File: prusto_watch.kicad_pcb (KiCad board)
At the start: 2 copper layers, 37.4 x 37.4 mm, 56 parts, among them J1 USB_microB_2040002-1, J2 Conn_02x05_Odd_Even, J3 Vibration Motor, J4 Conn_01x06, J5 Conn_01x06, J6 Conn_02x03_Odd_Even, J7 Conn_02x03_Counter_Clockwise, Q3 RUM002N02T2L, U1 STM32F303RCT6-48, U2 LTC4063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

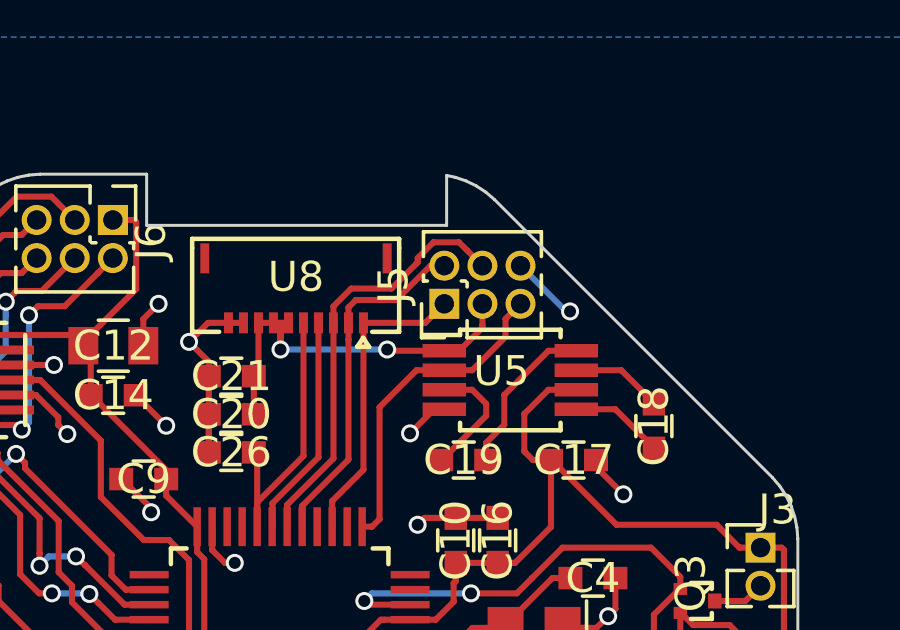
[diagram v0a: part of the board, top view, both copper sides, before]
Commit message: Breakout EXTCOMIN instead of 5Ven
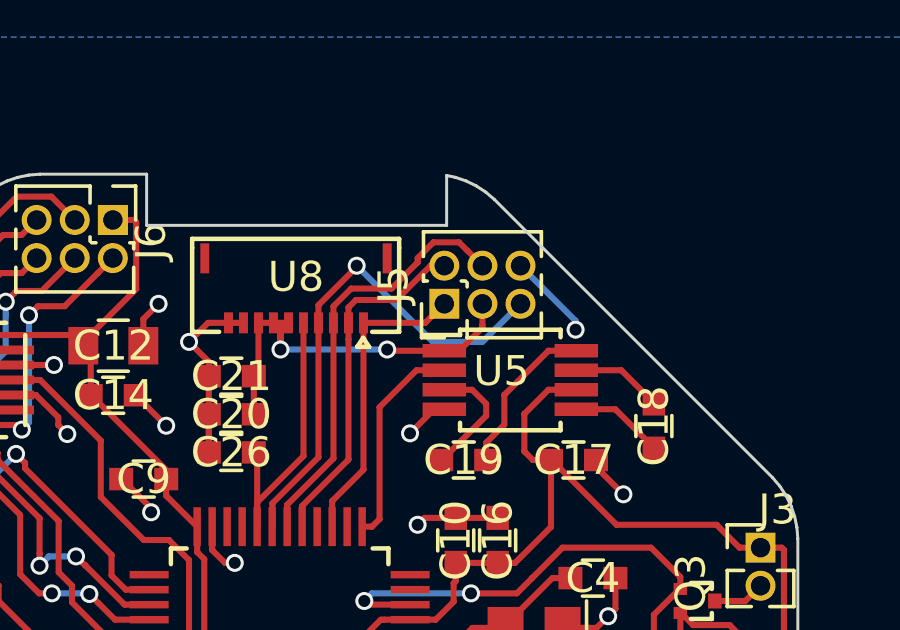
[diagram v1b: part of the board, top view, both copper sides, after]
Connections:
- J5 pad 5: /5V_EN -> /EXTCOMIN
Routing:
- net /EXTCOMIN: track 7.43 -> 17.1 mm, vias 0 -> 1
- net /5V_EN: track 10.9 -> 7.08 mm
- net GND: track 99.6 -> 100.2 mm
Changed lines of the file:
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@@
 (kicad_pcb (version 4) (host pcbnew 4.0.7)
   (general
-    (links 0)
+    (links 169)
     (no_connects 0)
     (area 127.356999 80.719059 164.868201 118.230261)
     (thickness 1.6)
     (drawings 80)
-    (tracks 791)
+    (tracks 795)
     (zones 0)
     (modules 56)
@@
       (net 26 /DISP_SCS))
     (pad 5 thru_hole oval (at 0 2.54 90) (size 1 1) (drill 0.65) (layers *.Cu *.Mask)
-      (net 30 /5V_EN))
+      (net 29 /EXTCOMIN))
     (pad 6 thru_hole oval (at 1.27 2.54 90) (size 1 1) (drill 0.65) (layers *.Cu *.Mask)
       (net 2 GND))
@@
       (xy -0.113933 2.757629) (xy -0.013056 2.757714) (xy 0 2.757714) (xy 0.10391 2.757652)) (layer B.SilkS) (width 0.01))
   )
-  (gr_text "Prusto Watch\nV0.4\nByron Wasti" (at 153.416 94.488 360) (layer B.SilkS)
+  (gr_text "Prusto Watch\nV0.4\nByron Wasti" (at 153.416 94.488) (layer B.SilkS)
     (effects (font (size 1.5 1.5) (thickness 0.3)) (justify left mirror))
   )
@@
     (effects (font (size 0.762 0.762) (thickness 0.1905)) (justify mirror))
   )
-  (gr_text GND (at 161.798 94.488 360) (layer B.SilkS)
+  (gr_text GND (at 161.798 94.488) (layer B.SilkS)
     (effects (font (size 0.762 0.762) (thickness 0.1905)) (justify mirror))
   )
@@
     (effects (font (size 0.762 0.762) (thickness 0.1905)) (justify mirror))
   )
-  (gr_text GND (at 130.302 94.742 360) (layer B.SilkS)
+  (gr_text GND (at 130.302 94.742) (layer B.SilkS)
     (effects (font (size 0.762 0.762) (thickness 0.1905)) (justify mirror))
   )
@@
   (segment (start 133.08 91.9425) (end 133.4332 91.9425) (width 0.2032) (layer F.Cu) (net 1))
   (via (at 133.785433 92.335751) (size 0.6) (drill 0.4) (layers F.Cu B.Cu) (net 1))
+  (segment (start 157.410267 85.655267) (end 157.410267 85.952188) (width 0.2032) (layer B.Cu) (net 2))
+  (segment (start 155.575 83.82) (end 157.410267 85.655267) (width 0.2032) (layer B.Cu) (net 2))
+  (via (at 157.410267 85.952188) (size 0.6) (drill 0.4) (layers F.Cu B.Cu) (net 2))
   (segment (start 157.969948 112.032051) (end 156.21 113.791999) (width 0.2032) (layer F.Cu) (net 2))
   (segment (start 156.21 113.791999) (end 156.21 114.3) (width 0.2032) (layer F.Cu) (net 2))
@@
   (via (at 144.526 86.36) (size 0.6) (drill 0.4) (layers F.Cu B.Cu) (net 2))
   (via (at 159.004 91.44) (size 0.6) (drill 0.4) (layers F.Cu B.Cu) (net 2))
-  (via (at 157.226 85.344) (size 0.6) (drill 0.4) (layers F.Cu B.Cu) (net 2))
   (via (at 151.892 89.408) (size 0.6) (drill 0.4) (layers F.Cu B.Cu) (net 2))
   (via (at 158.496 95.504) (size 0.6) (drill 0.4) (layers F.Cu B.Cu) (net 2))
@@
   (segment (start 142.144926 102.084) (end 142.388464 101.840462) (width 0.2032) (layer F.Cu) (net 2))
   (segment (start 163.83 106.7482) (end 162.8822 107.696) (width 0.2032) (layer F.Cu) (net 2))
-  (segment (start 157.099 85.344) (end 157.226 85.344) (width 0.2032) (layer B.Cu) (net 2))
   (segment (start 145.161 85.725) (end 144.526 86.36) (width 0.2032) (layer F.Cu) (net 2))
   (segment (start 163.83 106.045) (end 163.83 106.7482) (width 0.2032) (layer F.Cu) (net 2))
   (segment (start 132.7 93.205) (end 132.7 93.98) (width 0.2032) (layer F.Cu) (net 2))
-  (segment (start 155.575 83.82) (end 157.099 85.344) (width 0.2032) (layer B.Cu) (net 2))
   (segment (start 141.478 102.084) (end 142.144926 102.084) (width 0.2032) (layer F.Cu) (net 2))
   (segment (start 142.388464 101.840462) (end 142.688463 101.540463) (width 0.2032) (layer F.Cu) (net 2))
@@
   (segment (start 150.34 90.6218) (end 150.34 86.2782) (width 0.2032) (layer F.Cu) (net 28))
   (segment (start 150.34 86.2782) (end 150.34 85.725) (width 0.2032) (layer F.Cu) (net 28))
+  (segment (start 152.654 86.36) (end 154.305 86.36) (width 0.2032) (layer B.Cu) (net 29))
+  (segment (start 154.305 86.36) (end 155.575 85.09) (width 0.2032) (layer B.Cu) (net 29))
+  (segment (start 155.448 85.217) (end 155.575 85.09) (width 0.2032) (layer F.Cu) (net 29))
+  (segment (start 150.114 83.82) (end 152.654 86.36) (width 0.2032) (layer B.Cu) (net 29))
+  (segment (start 148.84 85.725) (end 148.84 85.132973) (width 0.2032) (layer F.Cu) (net 29))
+  (segment (start 148.84 85.132973) (end 150.114 83.858973) (width 0.2032) (layer F.Cu) (net 29))
+  (segment (start 150.114 83.858973) (end 150.114 83.82) (width 0.2032) (layer F.Cu) (net 29))
+  (via (at 150.114 83.82) (size 0.6) (drill 0.4) (layers F.Cu B.Cu) (net 29))
   (segment (start 148.84 85.725) (end 148.84 90.204831) (width 0.2032) (layer F.Cu) (net 29))
   (segment (start 148.84 90.204831) (end 147.305375 91.739456) (width 0.2032) (layer F.Cu) (net 29))
@@
   (segment (start 150.296 92.519) (end 150.6242 92.519) (width 0.2032) (layer F.Cu) (net 30))
   (segment (start 150.6242 92.519) (end 150.876 92.2672) (width 0.2032) (layer F.Cu) (net 30))
-  (segment (start 153.035 87.305) (end 153.9632 87.305) (width 0.2032) (layer F.Cu) (net 30))
-  (segment (start 153.9632 87.305) (end 155.075001 86.193199) (width 0.2032) (layer F.Cu) (net 30))
-  (segment (start 155.075001 85.589999) (end 155.575 85.09) (width 0.2032) (layer F.Cu) (net 30))
-  (segment (start 155.075001 86.193199) (end 155.075001 85.589999) (width 0.2032) (layer F.Cu) (net 30))
   (segment (start 143.196 94.619) (end 142.418078 94.619) (width 0.2032) (layer F.Cu) (net 31))
   (segment (start 142.418078 94.619) (end 141.942072 94.142994) (width 0.2032) (layer F.Cu) (net 31))

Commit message: Update silkscreen
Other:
- board text added: "GND SCS SDI EXT +5V SCK"
- board text removed: "GND SCS SDI 5en +5V SCK"
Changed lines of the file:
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@@
     (links 169)
     (no_connects 0)
-    (area 127.356999 80.719059 164.868201 118.230261)
+    (area 119.38 72.289635 175.206135 124.460001)
     (thickness 1.6)
     (drawings 80)
@@
     (effects (font (size 0.762 0.762) (thickness 0.1905)) (justify mirror))
   )
-  (gr_text "GND SCS SDI\n5en +5V SCK" (at 154.432 87.122) (layer B.SilkS)
+  (gr_text "GND SCS SDI\nEXT +5V SCK" (at 154.432 87.122) (layer B.SilkS)
     (effects (font (size 0.762 0.762) (thickness 0.1905)) (justify mirror))
   )

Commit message: Finish v0.4
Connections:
- U3 pad 13: (no net) -> GND
- U3 pad 15: (no net) -> GND
- U3 pad 16: (no net) -> GND
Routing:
- net GND: track 100.2 -> 103.2 mm, vias 38 -> 39
- net +3V3: track 151.9 -> 153.0 mm
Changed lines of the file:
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@@
 (kicad_pcb (version 4) (host pcbnew 4.0.7)
   (general
-    (links 169)
+    (links 172)
     (no_connects 0)
-    (area 119.38 72.289635 175.206135 124.460001)
+    (area 127.356999 80.719059 164.868201 118.230261)
     (thickness 1.6)
     (drawings 80)
-    (tracks 795)
+    (tracks 799)
     (zones 0)
     (modules 56)
@@
     (pad 4 smd rect (at -1.6 0.5) (size 1.2 0.3) (layers F.Cu F.Paste F.Mask)
       (net 31 /ACC_SCK))
-    (pad 15 smd rect (at 0 -1.5) (size 0.3 1.2) (layers F.Cu F.Paste F.Mask))
+    (pad 15 smd rect (at 0 -1.5) (size 0.3 1.2) (layers F.Cu F.Paste F.Mask)
+      (net 2 GND))
     (pad 5 smd rect (at -1.6 1) (size 1.2 0.3) (layers F.Cu F.Paste F.Mask)
       (net 2 GND))
-    (pad 13 smd rect (at 1.6 -1) (size 1.2 0.3) (layers F.Cu F.Paste F.Mask))
+    (pad 13 smd rect (at 1.6 -1) (size 1.2 0.3) (layers F.Cu F.Paste F.Mask)
+      (net 2 GND))
     (pad 12 smd rect (at 1.6 -0.5) (size 1.2 0.3) (layers F.Cu F.Paste F.Mask)
       (net 2 GND))
@@
     (pad 14 smd rect (at 0.5 -1.5) (size 0.3 1.2) (layers F.Cu F.Paste F.Mask)
       (net 8 +3V3))
-    (pad 16 smd rect (at -0.5 -1.5) (size 0.3 1.2) (layers F.Cu F.Paste F.Mask))
+    (pad 16 smd rect (at -0.5 -1.5) (size 0.3 1.2) (layers F.Cu F.Paste F.Mask)
+      (net 2 GND))
     (pad 7 smd rect (at 0 1.5) (size 0.3 1.2) (layers F.Cu F.Paste F.Mask)
       (net 34 /ACC_SDO))
@@
   (segment (start 133.08 91.9425) (end 133.4332 91.9425) (width 0.2032) (layer F.Cu) (net 1))
   (via (at 133.785433 92.335751) (size 0.6) (drill 0.4) (layers F.Cu B.Cu) (net 1))
+  (segment (start 138.76 86.63) (end 138.76 87.13) (width 0.2032) (layer F.Cu) (net 2))
+  (segment (start 136.398 85.09) (end 136.398 85.368) (width 0.2032) (layer F.Cu) (net 2))
+  (segment (start 136.66 85.352) (end 136.398 85.09) (width 0.2032) (layer F.Cu) (net 2))
+  (via (at 136.398 85.09) (size 0.6) (drill 0.4) (layers F.Cu B.Cu) (net 2))
+  (segment (start 136.66 86.13) (end 136.66 85.352) (width 0.2032) (layer F.Cu) (net 2))
+  (segment (start 136.398 85.368) (end 137.16 86.13) (width 0.2032) (layer F.Cu) (net 2))
   (segment (start 157.410267 85.655267) (end 157.410267 85.952188) (width 0.2032) (layer B.Cu) (net 2))
   (segment (start 155.575 83.82) (end 157.410267 85.655267) (width 0.2032) (layer B.Cu) (net 2))
@@
   (segment (start 133.6947 95.504) (end 133.4332 95.2425) (width 0.2032) (layer F.Cu) (net 7))
   (segment (start 135.128 99.543) (end 135.128 99.568) (width 0.2032) (layer F.Cu) (net 7))
+  (segment (start 137.66 85.3268) (end 137.66 86.13) (width 0.2032) (layer F.Cu) (net 8))
+  (segment (start 136.843798 84.510598) (end 137.66 85.3268) (width 0.2032) (layer F.Cu) (net 8))
+  (segment (start 136.119886 84.510598) (end 136.843798 84.510598) (width 0.2032) (layer F.Cu) (net 8))
+  (segment (start 135.56 85.070484) (end 136.119886 84.510598) (width 0.2032) (layer F.Cu) (net 8))
+  (segment (start 135.56 86.63) (end 135.56 85.070484) (width 0.2032) (layer F.Cu) (net 8))
   (segment (start 155.453207 105.415207) (end 155.448 105.415207) (width 0.2032) (layer F.Cu) (net 8))
   (segment (start 161.036 107.95) (end 158.501207 105.415207) (width 0.2032) (layer F.Cu) (net 8))
@@
   (segment (start 144.831 99.619) (end 145.034 99.416) (width 0.2032) (layer F.Cu) (net 8))
   (segment (start 143.196 99.619) (end 144.831 99.619) (width 0.2032) (layer F.Cu) (net 8))
-  (segment (start 137.66 85.3268) (end 137.66 86.13) (width 0.2032) (layer F.Cu) (net 8))
-  (segment (start 136.308745 85.228333) (end 137.561533 85.228333) (width 0.2032) (layer F.Cu) (net 8))
-  (segment (start 137.561533 85.228333) (end 137.66 85.3268) (width 0.2032) (layer F.Cu) (net 8))
-  (segment (start 135.56 85.977078) (end 136.308745 85.228333) (width 0.2032) (layer F.Cu) (net 8))
-  (segment (start 135.56 86.63) (end 135.56 85.977078) (width 0.2032) (layer F.Cu) (net 8))
   (segment (start 132.842 90.17) (end 132.842 86.911259) (width 0.2032) (layer F.Cu) (net 8))
   (segment (start 132.842 86.911259) (end 133.820208 85.933051) (width 0.2032) (layer F.Cu) (net 8))
@@
   (segment (start 150.296 92.519) (end 150.6242 92.519) (width 0.2032) (layer F.Cu) (net 30))
   (segment (start 150.6242 92.519) (end 150.876 92.2672) (width 0.2032) (layer F.Cu) (net 30))
+  (segment (start 139.446 82.296) (end 137.810812 83.931188) (width 0.2032) (layer F.Cu) (net 31))
+  (segment (start 137.810812 83.931188) (end 135.923196 83.931188) (width 0.2032) (layer F.Cu) (net 31))
+  (segment (start 134.732413 85.121971) (end 134.732413 85.546235) (width 0.2032) (layer F.Cu) (net 31))
+  (segment (start 135.923196 83.931188) (end 134.732413 85.121971) (width 0.2032) (layer F.Cu) (net 31))
   (segment (start 143.196 94.619) (end 142.418078 94.619) (width 0.2032) (layer F.Cu) (net 31))
   (segment (start 142.418078 94.619) (end 141.942072 94.142994) (width 0.2032) (layer F.Cu) (net 31))
@@
   (segment (start 141.942072 93.458902) (end 139.059995 90.576825) (width 0.2032) (layer F.Cu) (net 31))
   (segment (start 139.059995 90.576825) (end 139.059995 90.394003) (width 0.2032) (layer F.Cu) (net 31))
-  (segment (start 135.032412 85.246236) (end 134.732413 85.546235) (width 0.2032) (layer F.Cu) (net 31))
-  (segment (start 136.34746 83.931188) (end 135.032412 85.246236) (width 0.2032) (layer F.Cu) (net 31))
-  (segment (start 139.446 82.296) (end 138.946001 82.795999) (width 0.2032) (layer F.Cu) (net 31))
-  (segment (start 138.946001 82.795999) (end 138.33063 82.795999) (width 0.2032) (layer F.Cu) (net 31))
-  (segment (start 137.195441 83.931188) (end 136.34746 83.931188) (width 0.2032) (layer F.Cu) (net 31))
-  (segment (start 138.33063 82.795999) (end 137.195441 83.931188) (width 0.2032) (layer F.Cu) (net 31))
   (segment (start 136.311428 90.816197) (end 136.735692 90.816197) (width 0.2032) (layer F.Cu) (net 31))
   (segment (start 134.366 88.916078) (end 135.242783 89.792861) (width 0.2032) (layer F.Cu) (net 31))
